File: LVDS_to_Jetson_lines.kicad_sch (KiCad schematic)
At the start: 26 parts, among them IC1 SN74AVC4T245PWR, U5 TS3DDR3812_RUA_42, U6 TS3DDR3812_RUA_42, U8 SN74AVCH16T245_DGV_48

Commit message: a little cleanup
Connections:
- net FMC_LP_CSI_C_CLK_N renamed FMC_CSI_LP_C_CLK_N
- net FMC_LP_CSI_C_CLK_P renamed FMC_CSI_LP_C_CLK_P
- net FMC_LP_CSI_C_D0_N renamed FMC_CSI_LP_C_D0_N
- net FMC_LP_CSI_C_D0_P renamed FMC_CSI_LP_C_D0_P
- net FMC_LP_CSI_C_D1_N renamed FMC_CSI_LP_C_D1_N
- net FMC_LP_CSI_C_D1_P renamed FMC_CSI_LP_C_D1_P
- net FMC_LP_CSI_D_CLK_N renamed FMC_CSI_LP_D_CLK_N
- net FMC_LP_CSI_D_CLK_P renamed FMC_CSI_LP_D_CLK_P
- net FMC_LP_CSI_D_D0_N renamed FMC_CSI_LP_D_D0_N
- net FMC_LP_CSI_D_D0_P renamed FMC_CSI_LP_D_D0_P
- net FMC_LP_CSI_D_D1_N renamed FMC_CSI_LP_D_D1_N
- net FMC_LP_CSI_D_D1_P renamed FMC_CSI_LP_D_D1_P
- net LP_CSI_C_CLK_N renamed CSI_LP_C_CLK_N
- net LP_CSI_C_CLK_P renamed CSI_LP_C_CLK_P
- net LP_CSI_C_D0_N renamed CSI_LP_C_D0_N
- net LP_CSI_C_D0_P renamed CSI_LP_C_D0_P
- net LP_CSI_C_D1_N renamed CSI_LP_C_D1_N
- net LP_CSI_C_D1_P renamed CSI_LP_C_D1_P
- net LP_CSI_D_CLK_N renamed CSI_LP_D_CLK_N
- net LP_CSI_D_CLK_P renamed CSI_LP_D_CLK_P
- net LP_CSI_D_D0_N renamed CSI_LP_D_D0_N
- net LP_CSI_D_D0_P renamed CSI_LP_D_D0_P
- net LP_CSI_D_D1_N renamed CSI_LP_D_D1_N
- net LP_CSI_D_D1_P renamed CSI_LP_D_D1_P

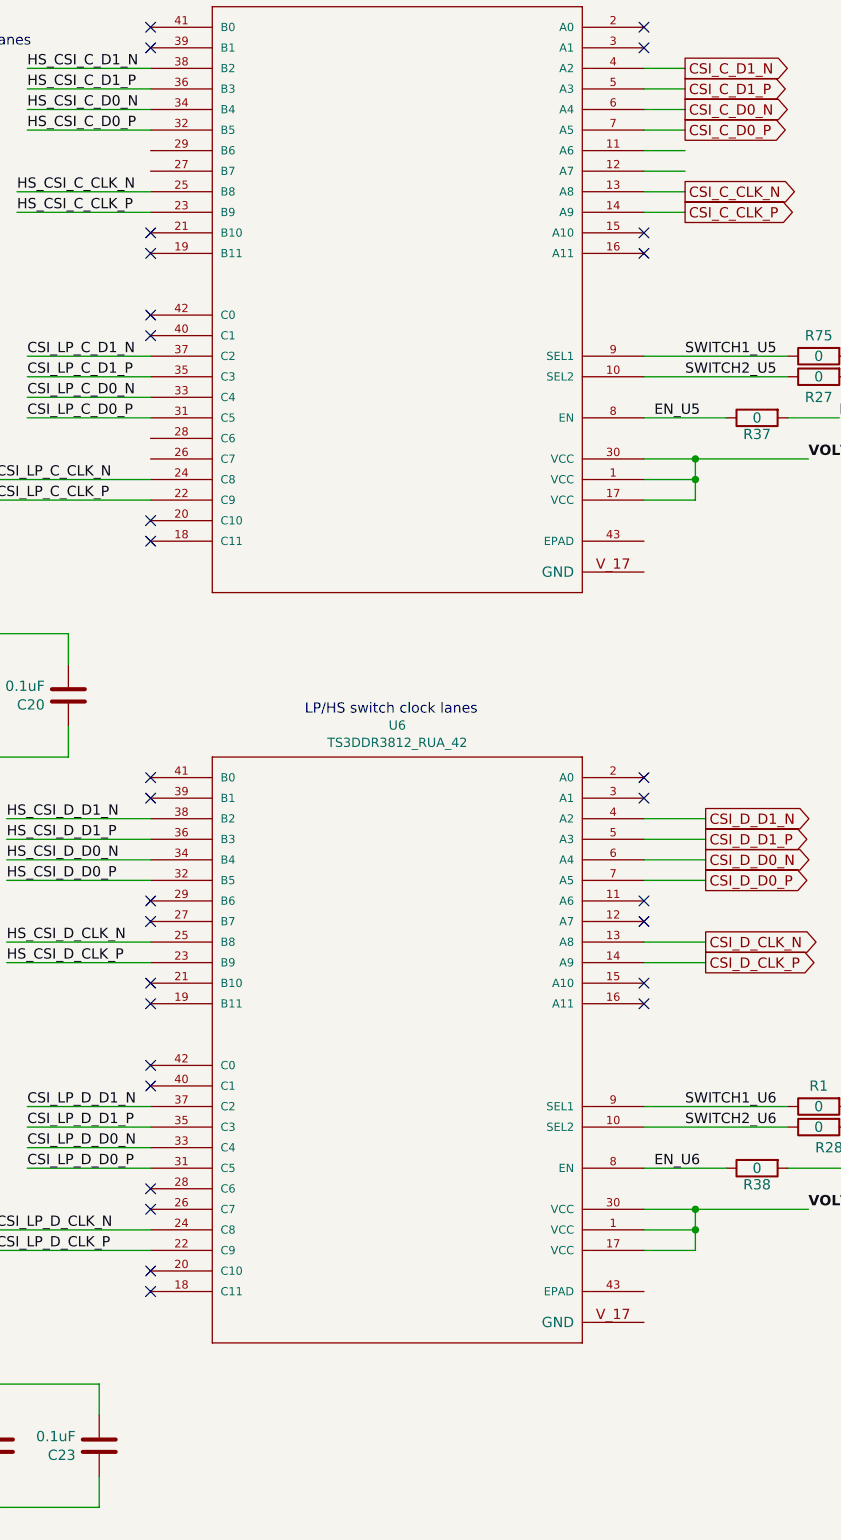
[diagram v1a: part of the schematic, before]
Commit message: DRC, ERC OK
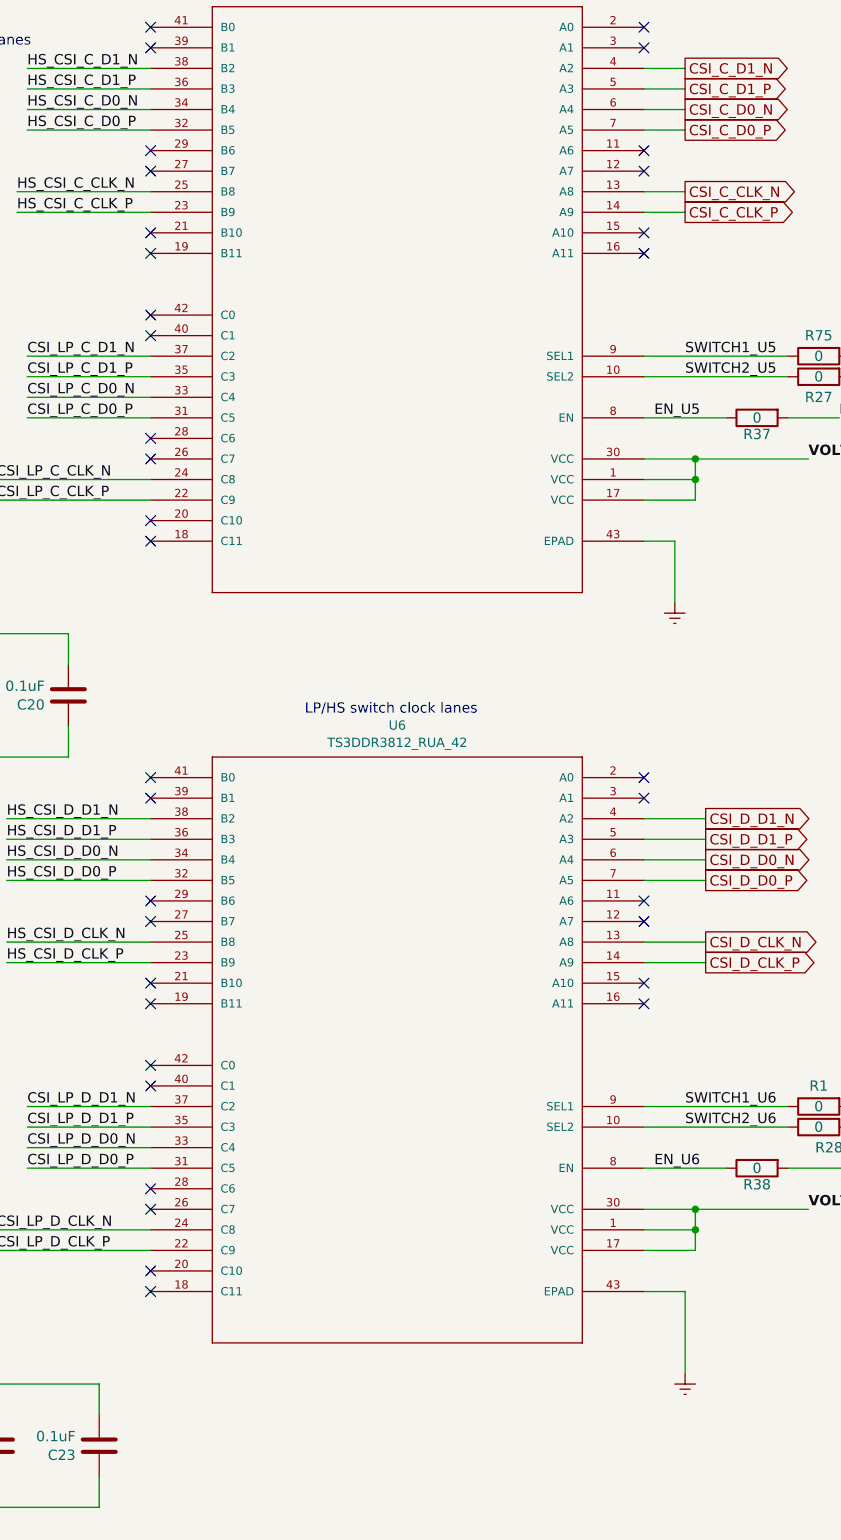
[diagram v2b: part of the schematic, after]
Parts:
- R1, R10, R2, R27, R28, R37, R38, R75: symbol FMC_MIPI_v2-rescue:R-Device -> FMC_MIPI_v2:R
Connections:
- removed net Earth: C1.1, C14.2, C15.2, C16.2, C17.2, C18.1, C19.1, C2.1, C20.1, C21.1, C22.1, C23.1, IC1.14 (2~{OE}), IC1.15 (1~{OE}), IC1.8 (GND), IC1.9 (GND), R10.2, U8.10 (GND_3), U8.11 (1B7), U8.12 (1B8), U8.13 (2B1), U8.14 (2B2), U8.15 (GND_4), U8.21 (GND_5), U8.25 (*2OE), U8.28 (GND_6), U8.34 (GND_7), U8.35 (2A2), U8.36 (2A1), U8.37 (1A8), U8.38 (1A7), U8.39 (GND_8), U8.4 (GND_2), U8.45 (GND), U8.48 (*1OE)
- new net: C14.2, C15.2
- new net: C16.2, C17.2
- new net: U8.10 (GND_3), U8.15 (GND_4), U8.21 (GND_5), U8.4 (GND_2)
- new net: U8.11 (1B7), U8.12 (1B8), U8.13 (2B1), U8.14 (2B2)
- new net: U8.25 (*2OE), U8.28 (GND_6), U8.34 (GND_7), U8.39 (GND_8), U8.45 (GND), U8.48 (*1OE)
- new net: U8.35 (2A2), U8.36 (2A1), U8.37 (1A8), U8.38 (1A7)
- new net: C18.1, C19.1, C20.1
- new net: IC1.14 (2~{OE}), IC1.15 (1~{OE}), IC1.8 (GND), IC1.9 (GND)
- new net: C21.1, C22.1, C23.1
- no-connect marks 30 -> 36
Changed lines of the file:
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@@
   )
   (no_connect (at 306.07 210.82))
+  (no_connect (at 367.03 82.55))
+  (no_connect (at 306.07 115.57))
   (no_connect (at 306.07 193.04))
   (no_connect (at 306.07 100.33))
+  (no_connect (at 306.07 118.11))
   (no_connect (at 306.07 218.44))
   (no_connect (at 367.03 185.42))
+  (no_connect (at 306.07 82.55))
   (no_connect (at 306.07 220.98))
   (no_connect (at 306.07 90.17))
   (no_connect (at 306.07 67.31))
   (no_connect (at 306.07 64.77))
+  (no_connect (at 306.07 80.01))
   (no_connect (at 306.07 185.42))
   (no_connect (at 367.03 64.77))
@@
   (no_connect (at 306.07 160.02))
   (no_connect (at 306.07 182.88))
+  (no_connect (at 367.03 80.01))
   (no_connect (at 367.03 67.31))
   (wire (pts (xy 373.38 118.11) (xy 373.38 120.65))
@@
     (stroke (width 0) (type default) (color 0 0 0 0))
   )
+  (wire (pts (xy 372.11 220.98) (xy 372.11 231.14))
+    (stroke (width 0) (type default) (color 0 0 0 0))
+  )
   (wire (pts (xy 52.07 78.74) (xy 49.53 78.74))
     (stroke (width 0) (type default) (color 0 0 0 0))
@@
     (stroke (width 0) (type default) (color 0 0 0 0))
   )
+  (wire (pts (xy 367.03 128.27) (xy 370.84 128.27))
+    (stroke (width 0) (type default) (color 0 0 0 0))
+  )
   (wire (pts (xy 102.87 228.6) (xy 81.28 228.6))
     (stroke (width 0) (type default) (color 0 0 0 0))
@@
     (stroke (width 0) (type default) (color 0 0 0 0))
   )
-  (wire (pts (xy 367.03 82.55) (xy 372.11 82.55))
-    (stroke (width 0) (type default) (color 0 0 0 0))
-  )
   (wire (pts (xy 173.99 185.42) (xy 173.99 189.23))
     (stroke (width 0) (type default) (color 0 0 0 0))
@@
     (stroke (width 0) (type default) (color 0 0 0 0))
   )
-  (wire (pts (xy 367.03 80.01) (xy 372.11 80.01))
-    (stroke (width 0) (type default) (color 0 0 0 0))
-  )
   (wire (pts (xy 163.83 193.04) (xy 173.99 193.04))
     (stroke (width 0) (type default) (color 0 0 0 0))
@@
     (stroke (width 0) (type default) (color 0 0 0 0))
   )
+  (wire (pts (xy 367.03 220.98) (xy 372.11 220.98))
+    (stroke (width 0) (type default) (color 0 0 0 0))
+  )
   (wire (pts (xy 86.36 74.93) (xy 86.36 72.39))
     (stroke (width 0) (type default) (color 0 0 0 0))
@@
   )
   (wire (pts (xy 162.56 31.75) (xy 185.42 31.75))
+    (stroke (width 0) (type default) (color 0 0 0 0))
+  )
+  (wire (pts (xy 370.84 128.27) (xy 370.84 135.89))
     (stroke (width 0) (type default) (color 0 0 0 0))
   )
@@
     (pin "8")
     (pin "9")
-    (pin "V")
-    (pin "V_1")
-    (pin "V_10")
-    (pin "V_11")
-    (pin "V_12")
-    (pin "V_13")
-    (pin "V_14")
-    (pin "V_15")
-    (pin "V_16")
-    (pin "V_17")
-    (pin "V_17")
-    (pin "V_2")
-    (pin "V_3")
-    (pin "V_4")
-    (pin "V_5")
-    (pin "V_6")
-    (pin "V_7")
-    (pin "V_8")
-    (pin "V_9")
   )
   (symbol (lib_id "FMC_MIPI_v2:Earth") (at 109.22 167.64 0) (unit 1)
@@
     (pin "1")
   )
-  (symbol (lib_id "FMC_MIPI_v2-rescue:R-Device") (at 388.62 105.41 90) (mirror x) (unit 1)
+  (symbol (lib_id "FMC_MIPI_v2:R") (at 388.62 105.41 90) (mirror x) (unit 1)
     (in_bom yes) (on_board yes)
     (property "Reference" "R75" (id 0) (at 388.62 102.87 90))
@@
     (pin "8")
     (pin "9")
-    (pin "V")
-    (pin "V_1")
-    (pin "V_10")
-    (pin "V_11")
-    (pin "V_12")
-    (pin "V_13")
-    (pin "V_14")
-    (pin "V_15")
-    (pin "V_16")
-    (pin "V_17")
-    (pin "V_17")
-    (pin "V_2")
-    (pin "V_3")
-    (pin "V_4")
-    (pin "V_5")
-    (pin "V_6")
-    (pin "V_7")
-    (pin "V_8")
-    (pin "V_9")
   )
   (symbol (lib_id "FMC_MIPI_v2:Earth") (at 165.1 176.53 0) (unit 1)
@@
     (pin "1")
   )
-  (symbol (lib_id "FMC_MIPI_v2-rescue:R-Device") (at 91.44 259.08 0) (mirror y) (unit 1)
+  (symbol (lib_id "FMC_MIPI_v2:R") (at 91.44 259.08 0) (mirror y) (unit 1)
     (in_bom yes) (on_board yes)
     (property "Reference" "R10" (id 0) (at 93.98 259.08 90))
@@
     (pin "2")
   )
-  (symbol (lib_id "FMC_MIPI_v2-rescue:R-Device") (at 381 113.03 90) (mirror x) (unit 1)
+  (symbol (lib_id "FMC_MIPI_v2:R") (at 381 113.03 90) (mirror x) (unit 1)
     (in_bom yes) (on_board yes)
     (property "Reference" "R37" (id 0) (at 381 115.062 90))
@@
     (pin "1")
   )
-  (symbol (lib_id "FMC_MIPI_v2-rescue:R-Device") (at 36.83 67.31 90) (mirror x) (unit 1)
+  (symbol (lib_id "FMC_MIPI_v2:R") (at 36.83 67.31 90) (mirror x) (unit 1)
     (in_bom yes) (on_board yes)
     (property "Reference" "R2" (id 0) (at 36.83 64.77 90))
@@
     (pin "9")
   )
-  (symbol (lib_id "FMC_MIPI_v2-rescue:R-Device") (at 388.62 198.12 90) (mirror x) (unit 1)
+  (symbol (lib_id "FMC_MIPI_v2:R") (at 388.62 198.12 90) (mirror x) (unit 1)
     (in_bom yes) (on_board yes)
     (property "Reference" "R1" (id 0) (at 388.62 195.58 90))
@@
     (pin "2")
   )
-  (symbol (lib_id "FMC_MIPI_v2-rescue:R-Device") (at 388.62 107.95 90) (mirror x) (unit 1)
+  (symbol (lib_id "FMC_MIPI_v2:R") (at 388.62 107.95 90) (mirror x) (unit 1)
     (in_bom yes) (on_board yes)
     (property "Reference" "R27" (id 0) (at 388.62 110.49 90))
@@
     (pin "1")
   )
-  (symbol (lib_id "FMC_MIPI_v2-rescue:R-Device") (at 388.62 200.66 90) (mirror x) (unit 1)
+  (symbol (lib_id "FMC_MIPI_v2:R") (at 388.62 200.66 90) (mirror x) (unit 1)
     (in_bom yes) (on_board yes)
     (property "Reference" "R28" (id 0) (at 389.89 203.2 90))
@@
     (pin "2")
   )
-  (symbol (lib_id "FMC_MIPI_v2-rescue:R-Device") (at 381 205.74 90) (mirror x) (unit 1)
+  (symbol (lib_id "FMC_MIPI_v2:R") (at 381 205.74 90) (mirror x) (unit 1)
     (in_bom yes) (on_board yes)
     (property "Reference" "R38" (id 0) (at 381 207.772 90))
@@
     (pin "2")
   )
+  (symbol (lib_id "FMC_MIPI_v2:Earth") (at 370.84 135.89 0) (unit 1)
+    (in_bom yes) (on_board yes)
+    (property "Reference" "#PWR0172" (id 0) (at 370.84 142.24 0)
+      (effects (font (size 1.27 1.27)) hide)
+    )
+    (property "Value" "Earth" (id 1) (at 370.84 139.7 0)
+      (effects (font (size 1.27 1.27)) hide)
+    )
+    (property "Footprint" "" (id 2) (at 370.84 135.89 0)
+      (effects (font (size 1.27 1.27)) hide)
+    )
+    (property "Datasheet" "~" (id 3) (at 370.84 135.89 0)
+      (effects (font (size 1.27 1.27)) hide)
+    )
+    (pin "1")
+  )
+  (symbol (lib_id "FMC_MIPI_v2:Earth") (at 372.11 231.14 0) (unit 1)
+    (in_bom yes) (on_board yes)
+    (property "Reference" "#PWR0171" (id 0) (at 372.11 237.49 0)
+      (effects (font (size 1.27 1.27)) hide)
+    )
+    (property "Value" "Earth" (id 1) (at 372.11 234.95 0)
+      (effects (font (size 1.27 1.27)) hide)
+    )
+    (property "Footprint" "" (id 2) (at 372.11 231.14 0)
+      (effects (font (size 1.27 1.27)) hide)
+    )
+    (property "Datasheet" "~" (id 3) (at 372.11 231.14 0)
+      (effects (font (size 1.27 1.27)) hide)
+    )
+    (pin "1")
+  )
   (sheet (at 184.15 64.77) (size 31.75 8.89) (fields_autoplaced)

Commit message: All warnings fixed
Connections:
- net Earth: now reaches U6.43 (EPAD)
- net Earth: now also C1.1, C14.2, C15.2, C16.2, C17.2, C18.1, C19.1, C2.1, C20.1, C21.1, C22.1, C23.1, IC1.14 (2~{OE}), IC1.15 (1~{OE}), IC1.8 (GND), IC1.9 (GND), R10.2, U5.43 (EPAD), U8.10 (GND_3), U8.11 (1B7), U8.12 (1B8), U8.13 (2B1), U8.14 (2B2), U8.15 (GND_4), U8.21 (GND_5), U8.25 (*2OE), U8.28 (GND_6), U8.34 (GND_7), U8.35 (2A2), U8.36 (2A1), U8.37 (1A8), U8.38 (1A7), U8.39 (GND_8), U8.4 (GND_2), U8.45 (GND), U8.48 (*1OE)

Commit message: JLCPCB BOM OK
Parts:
- C1: LCSC (none) -> C1525; Part Number TMK105BJ104KV-F -> CL05B104KO5NNNC
- C14, C15, C16, C18, C19, C2, C21, C22: LCSC (none) -> C1525
- IC1: LCSC (none) -> C81461
- JP2, JP3: LCSC (none) -> DnP
- R1, R27, R28, R37, R38, R75: LCSC (none) -> C17477; Part Number RC0805JR-070RL -> 0805W8F0000T5E
- R2: LCSC (none) -> C17673
- U5, U6: LCSC (none) -> NeedToAsk
- U8: value SN74AVCH16T245_DGV_48 -> SN74AVCH16T245GR; footprint FMC_MIPI_v2_sym:DGV48 -> FMC_MIPI_v2_sym:SOP50P810X120-48N; LCSC (none) -> C181413

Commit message: All DRC, ERC and BOM are good
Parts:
- U8: footprint FMC_MIPI_v2_sym:SOP50P810X120-48N -> SOP50P810X120-48N; symbol FMC_MIPI_v2:SN74AVCH16T245_DGV_48 -> FMC_MIPI_v2:SN74AVCH16T245GR; Height (none) -> 1.2; Manufacturer_Name (none) -> Texas Instruments; Manufacturer_Part_Number (none) -> SN74AVCH16T245GR; Mouser Part Number (none) -> 595-SN74AVCH16T245GR; Mouser Price/Stock (none) -> https://www.mouser.co.uk/ProductDetail/Texas-Instruments/SN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
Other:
- moved on the sheet: C16, C17

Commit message: Generated BOM, before Gerbers generation
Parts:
- U5, U6: LCSC NeedToAsk -> C181266
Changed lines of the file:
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@@
       (effects (font (size 1.524 1.524)) hide)
     )
-    (property "LCSC" "NeedToAsk" (id 4) (at 308.61 157.48 0)
+    (property "LCSC" "C181266" (id 4) (at 308.61 157.48 0)
       (effects (font (size 1.27 1.27)) hide)
     )
@@
       (effects (font (size 1.524 1.524)) hide)
     )
-    (property "LCSC" "NeedToAsk" (id 4) (at 308.61 64.77 0)
+    (property "LCSC" "C181266" (id 4) (at 308.61 64.77 0)
       (effects (font (size 1.27 1.27)) hide)
     )
